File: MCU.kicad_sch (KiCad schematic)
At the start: 28 parts, among them J2 USB_C_Receptacle_USB2.0_16P, J8 FTSH-105-01-L-DV-K-A, U1 STM32H743VITx, Y1 Crystal_GND24

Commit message: LCD connector, backlight, other work
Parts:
- removed C12: 100n, Capacitor_SMD:C_0603_1608Metric_Pad1.08x0.95mm_HandSolder, symbol Device:C
- removed R5: 5.1k, Resistor_SMD:R_0603_1608Metric_Pad0.98x0.95mm_HandSolder, symbol Device:R
- removed S3: RKB2SJM250SMTR_LFS, RKB2SJM250SMTRLFS, symbol SamacSys_Parts:RKB2SJM250SMTR_LFS
- added C16, C17: 2.2u, Capacitor_SMD:C_0603_1608Metric_Pad1.08x0.95mm_HandSolder, symbol Device:C
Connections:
- net GND: now also U1.10 (VSS), U1.19 (VSSA), U1.26 (VSS), U1.49 (VSS), U1.74 (VSS), U1.99 (VSS), C16.2, C17.2
- net at U1.48 (VCAP): now also C17.1
- net at U1.73 (VCAP): now also C16.1
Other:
- removed sheet Indicator LED 1
- removed sheet Indicator LED 2

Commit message: preliminary complete schematic
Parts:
- added C33: 100n, Capacitor_SMD:C_0603_1608Metric_Pad1.08x0.95mm_HandSolder, symbol Device:C
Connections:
- net SWO is gone; now on net I2S_BCLK: J8.6
- net +3.3V: now also U1.100 (VDD), U1.11 (VDD), U1.27 (VDD), U1.50 (VDD), U1.75 (VDD), C33.1
- net BOOT0: now also U1.93 (PB7), U1.94 (BOOT0)
- net GND: now also C33.2
- net HSE_IN: now also U1.12 (PH0)
- net HSE_OUT: now also U1.13 (PH1)
- net NRST: now also U1.14 (NRST)
- net SWD_CLK: now also U1.76 (PA14)
- net SWD_IO: now also U1.72 (PA13)
- net USB+: now also U1.71 (PA12)
- net USB-: now also U1.70 (PA11)
- net LCD_R5: now reaches U1.15 (PC0)
- net SD_MOSI: now reaches U1.16 (PC1)
- net DPAD_A0: now reaches U1.17 (PC2_C)
- net DPAD_A1: now reaches U1.18 (PC3_C)
- net VDDA: now reaches U1.20 (VREF+)
- net VDDA: now also U1.21 (VDDA)
- net LCD_R2: now reaches U1.23 (PA1)
- net LCD_R1: now reaches U1.24 (PA2)
- net LCD_B5: now reaches U1.25 (PA3)
- net LCD_VSYNC: now reaches U1.28 (PA4)
- net LCD_R4: now reaches U1.29 (PA5)
- net LCD_G2: now reaches U1.30 (PA6)
- net I2S_SD: now reaches U1.31 (PA7)
- net V_SENSE_5: now reaches U1.32 (PC4)
- net LCD_R3: now reaches U1.34 (PB0)
- net V_SENSE_12: now reaches U1.35 (PB1)
- net BKLT_CTRL: now reaches U1.39 (PE9)
- net LCD_G3: now reaches U1.41 (PE11)
- net LCD_B4: now reaches U1.42 (PE12)
- net LCD_DE: now reaches U1.43 (PE13)
- net LCD_CLK: now reaches U1.44 (PE14)
- net LCD_R7: now reaches U1.45 (PE15)
- net LCD_G4: now reaches U1.46 (PB10)
- net LCD_G5: now reaches U1.47 (PB11)
- net SD_SCK: now reaches U1.52 (PB13)
- net SD_SCK: now also U1.80 (PC12)
- net SD_MISO: now reaches U1.53 (PB14)
- net SD_CS: now reaches U1.54 (PB15)
- net SD_WP: now reaches U1.55 (PD8)
- net SD_CD: now reaches U1.56 (PD9)
- net LCD_B3: now reaches U1.57 (PD10)
- net LCD_EN: now reaches U1.58 (PD11)
- net CTP_SCL: now reaches U1.59 (PD12)
- net CTP_SDA: now reaches U1.60 (PD13)
- net CTP_INT: now reaches U1.61 (PD14)
- net CTP_RST: now reaches U1.62 (PD15)
- net LCD_HSYNC: now reaches U1.63 (PC6)
- net LCD_G6: now reaches U1.64 (PC7)
- net SD_D0: now reaches U1.65 (PC8)
- net SD_D1: now reaches U1.66 (PC9)
- net LCD_R6: now reaches U1.67 (PA8)
- net I2S_WS: now reaches U1.77 (PA15)
- net SD_D2: now reaches U1.78 (PC10)
- net SD_D3: now reaches U1.79 (PC11)
- net DPAD_RX: now reaches U1.81 (PD0)
- net DPAD_TX: now reaches U1.82 (PD1)
- net SD_CMD: now reaches U1.83 (PD2)
- net LCD_G7: now reaches U1.84 (PD3)
- net LCD_B2: now reaches U1.87 (PD6)
- net I2S_BCLK: now reaches U1.89 (PB3)
- net LCD_B6: now reaches U1.95 (PB8)
- net LCD_B7: now reaches U1.96 (PB9)
- no-connect marks 4 -> 30

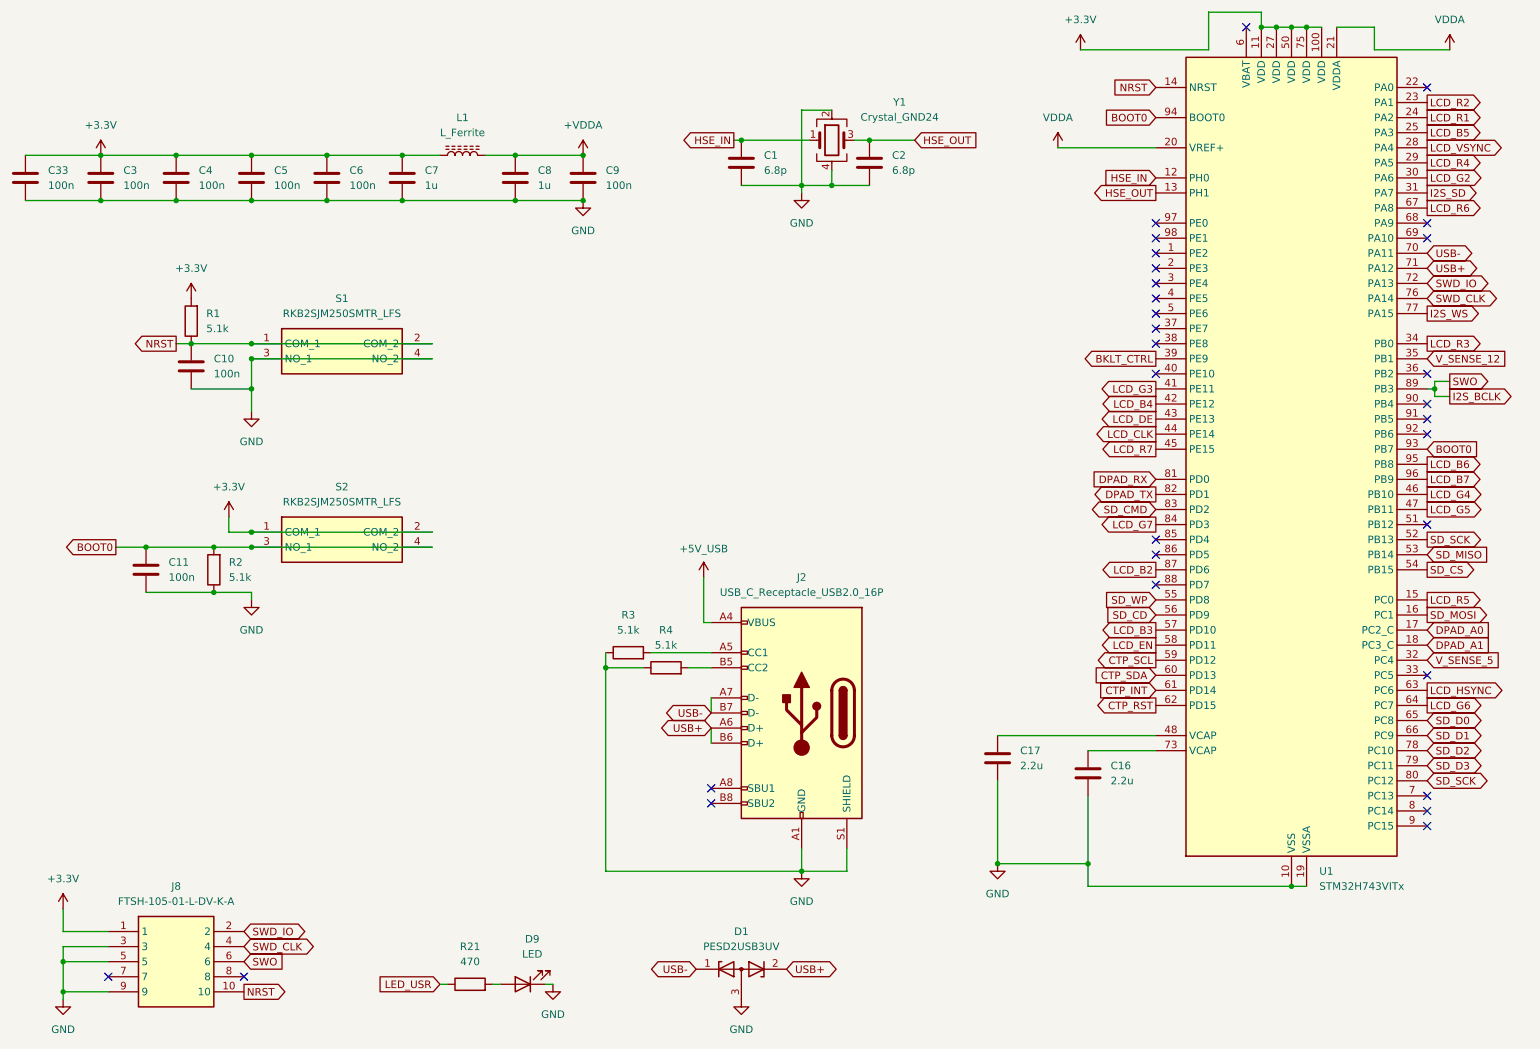
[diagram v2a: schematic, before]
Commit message: basic layout organization, fix +VDDA typo
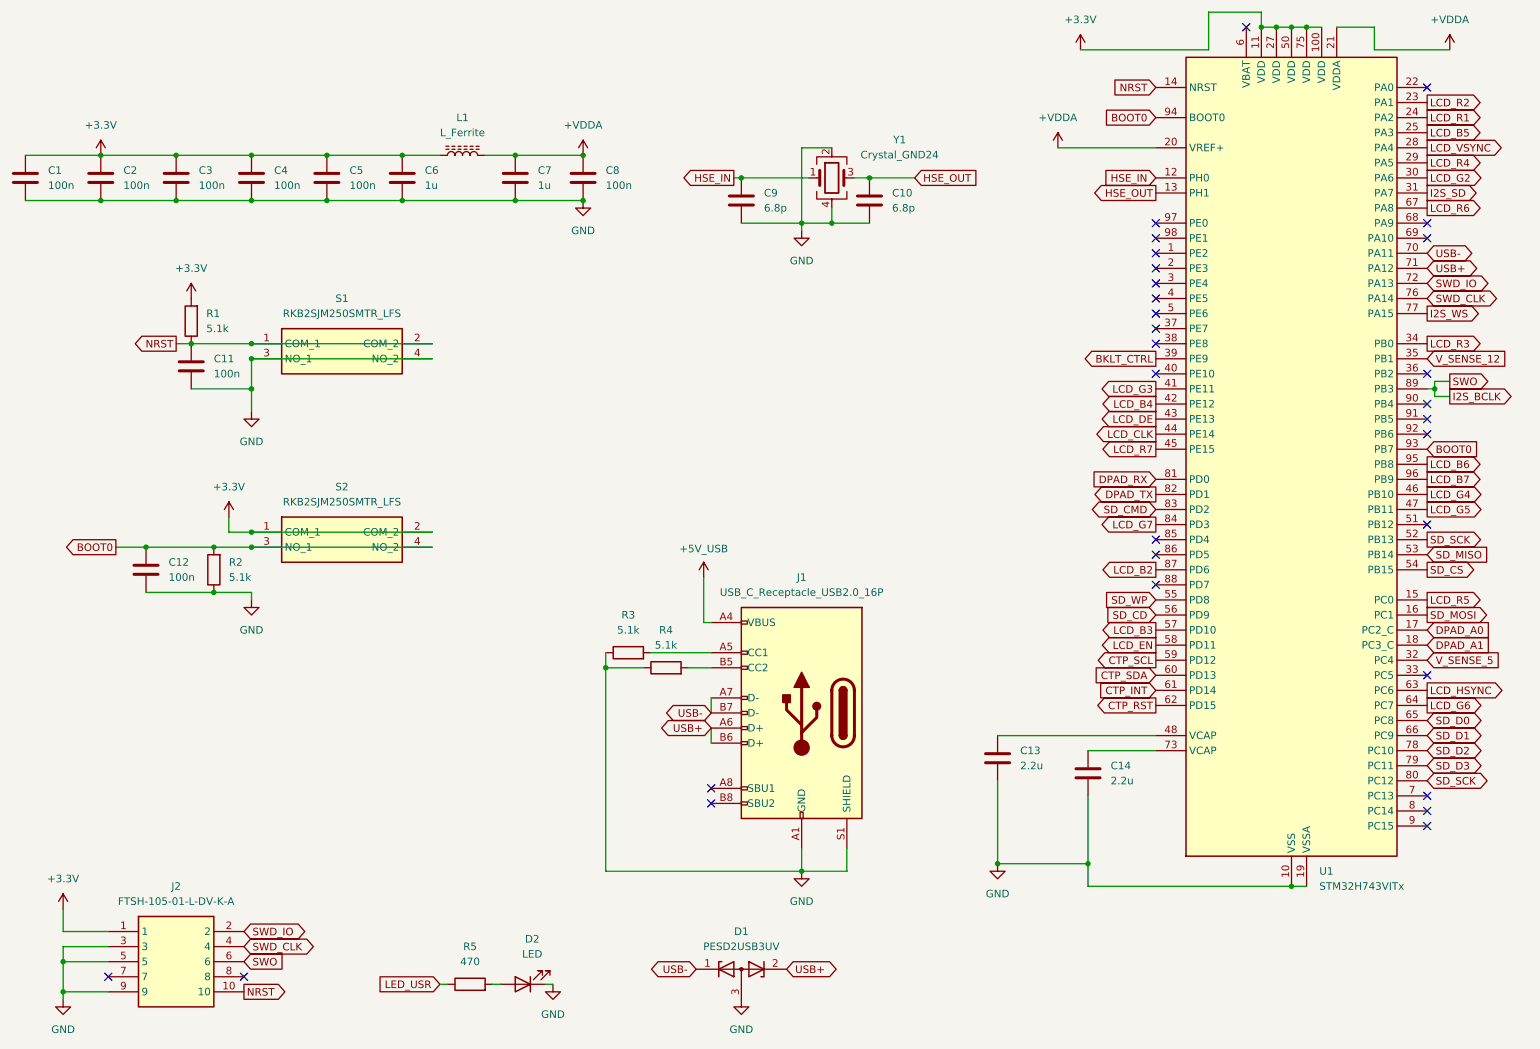
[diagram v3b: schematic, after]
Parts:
- renumbered C33 to C1, C2 to C10, C10 to C11, C11 to C12, C17 to C13, C16 to C14, C3 to C2, C4 to C3, C5 to C4, C6 to C5, C7 to C6, C8 to C7, C9 to C8, C1 to C9, D9 to D2, J2 to J1, J8 to J2, R21 to R5
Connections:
- net VDDA is gone; now on net +VDDA: U1.20 (VREF+), U1.21 (VDDA)
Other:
- moved on the sheet: C10, C9, Y1

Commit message: full preliminary layout
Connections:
- net FDCAN2_RX: now reaches U1.51 (PB12)
- net FDCAN2_TX: now reaches U1.92 (PB6)
- no-connect marks 30 -> 28
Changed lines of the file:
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@@
-	)
-	(no_connect
-		(at 261.62 85.09)
 	)
 	(no_connect
@@
 	(no_connect
 		(at 261.62 125.73)
-	)
-	(no_connect
-		(at 261.62 100.33)
 	)
 	(no_connect
@@
 		)
 	)
+	(global_label "FDCAN2_RX"
+		(shape input)
+		(at 261.62 100.33 0)
+		(fields_autoplaced yes)
+		(effects
+			(font
+				(size 1.27 1.27)
+			)
+			(justify left)
+		)
+		(property "Intersheetrefs" "${INTERSHEET_REFS}"
+			(at 275.3095 100.33 0)
+			(effects
+				(font
+					(size 1.27 1.27)
+				)
+				(justify left)
+				(hide yes)
+			)
+		)
+	)
 	(global_label "BOOT0"
 		(shape input)
@@
 			(effects
 				(font
+					(size 1.27 1.27)
+				)
+				(justify left)
+				(hide yes)
+			)
+		)
+	)
+	(global_label "FDCAN2_TX"
+		(shape output)
+		(at 261.62 85.09 0)
+		(fields_autoplaced yes)
+		(effects
+			(font
+				(size 1.27 1.27)
+			)
+			(justify left)
+		)
+		(property "Intersheetrefs" "${INTERSHEET_REFS}"
+			(at 275.0071 85.09 0)
+			(effects
+				(font

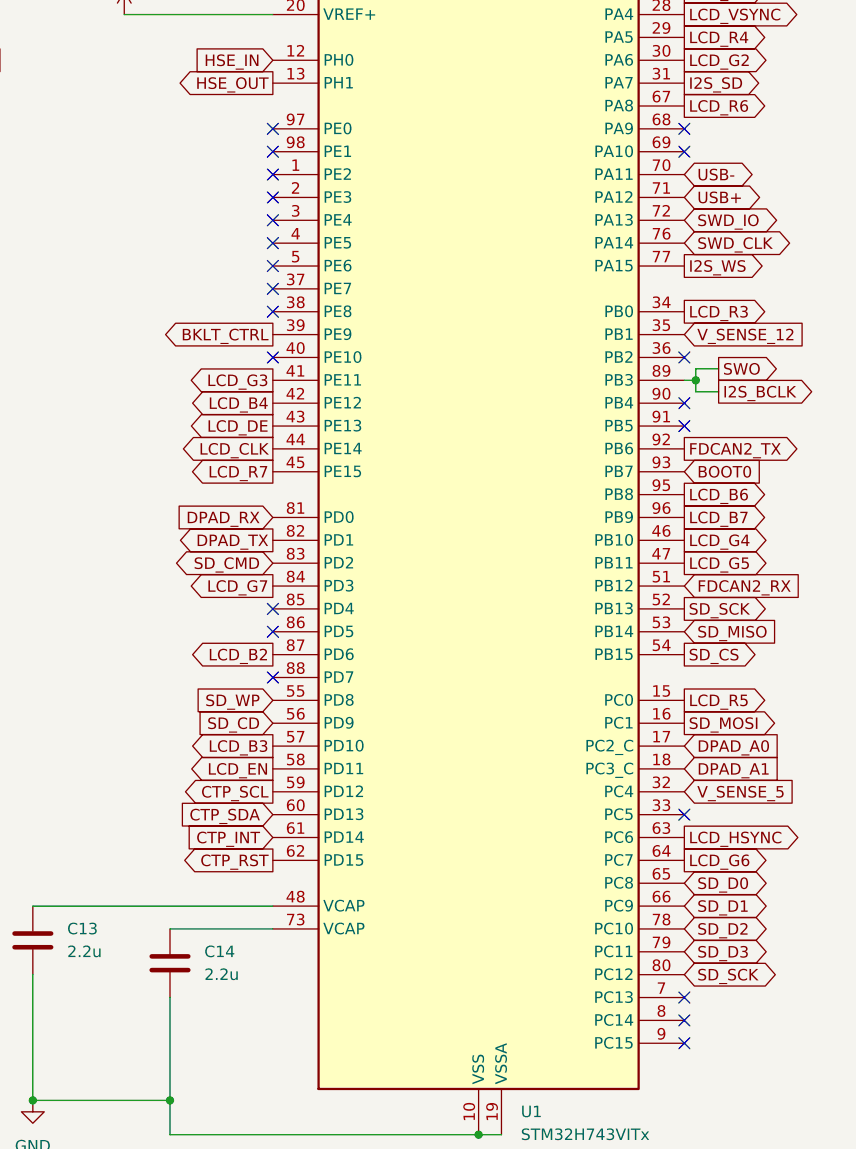
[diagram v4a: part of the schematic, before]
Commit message: 3.3v regulator changes, GPIO output fixes, layout changes
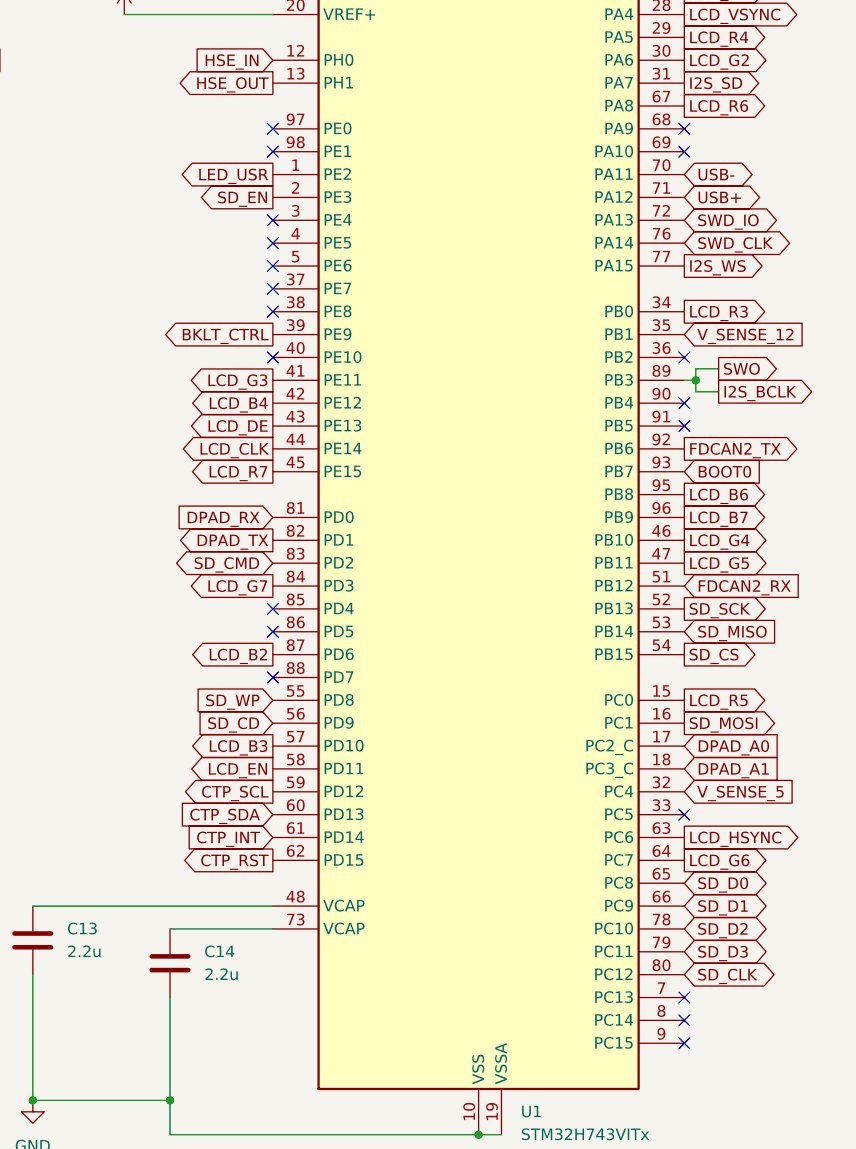
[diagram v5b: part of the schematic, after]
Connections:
- net LED_USR: now also U1.1 (PE2)
- net SD_SCK: no longer U1.80 (PC12)
- net SD_EN: now reaches U1.2 (PE3)
- new net SD_CLK: U1.80 (PC12)
- no-connect marks 28 -> 26
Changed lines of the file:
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@@
-	)
-	(no_connect
-		(at 215.9 57.15)
 	)
 	(no_connect
@@
 	(no_connect
 		(at 261.62 74.93)
-	)
-	(no_connect
-		(at 215.9 54.61)
 	)
 	(no_connect
@@
 		)
 	)
+	(global_label "LED_USR"
+		(shape output)
+		(at 215.9 54.61 180)
+		(fields_autoplaced yes)
+		(effects
+			(font
+				(size 1.27 1.27)
+			)
+			(justify right)
+		)
+		(property "Intersheetrefs" "${INTERSHEET_REFS}"
+			(at 204.6901 54.61 0)
+			(effects
+				(font
+					(size 1.27 1.27)
+				)
+				(justify right)
+				(hide yes)
+			)
+		)
+	)
 	(global_label "SD_MISO"
 		(shape input)
@@
 		)
 	)
+	(global_label "SD_EN"
+		(shape output)
+		(at 215.9 57.15 180)
+		(fields_autoplaced yes)
+		(effects
+			(font
+				(size 1.27 1.27)
+			)
+			(justify right)
+		)
+		(property "Intersheetrefs" "${INTERSHEET_REFS}"
+			(at 206.9882 57.15 0)
+			(effects
+				(font
+					(size 1.27 1.27)
+				)
+				(justify right)
+				(hide yes)
+			)
+		)
+	)
 	(global_label "HSE_IN"
 		(shape input)
@@
 		)
 	)
-	(global_label "SD_SCK"
+	(global_label "SD_CLK"
 		(shape bidirectional)
 		(at 261.62 143.51 0)
@@
 		)
 		(property "Intersheetrefs" "${INTERSHEET_REFS}"
-			(at 272.9131 143.51 0)
-			(effects
-				(font
+			(at 272.7317 143.51 0)
+			(effects
+				(font

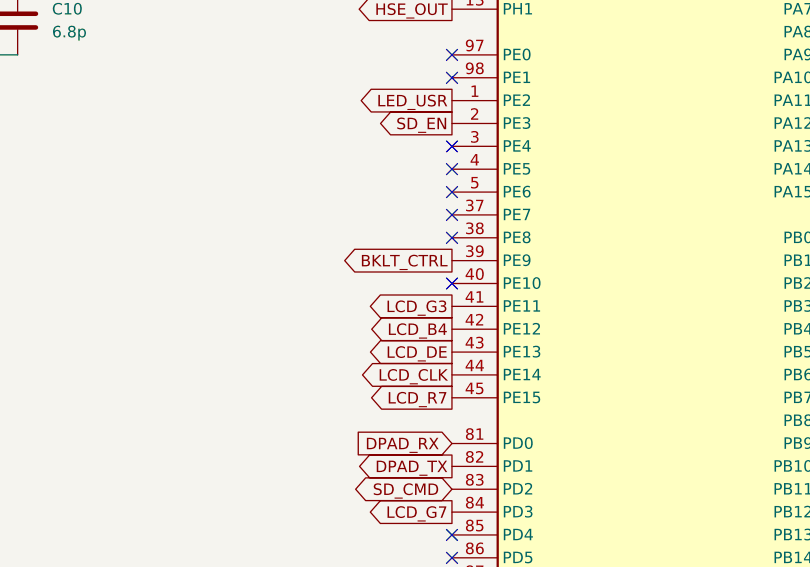
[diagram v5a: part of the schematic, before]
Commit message: finalized schematic, some routing
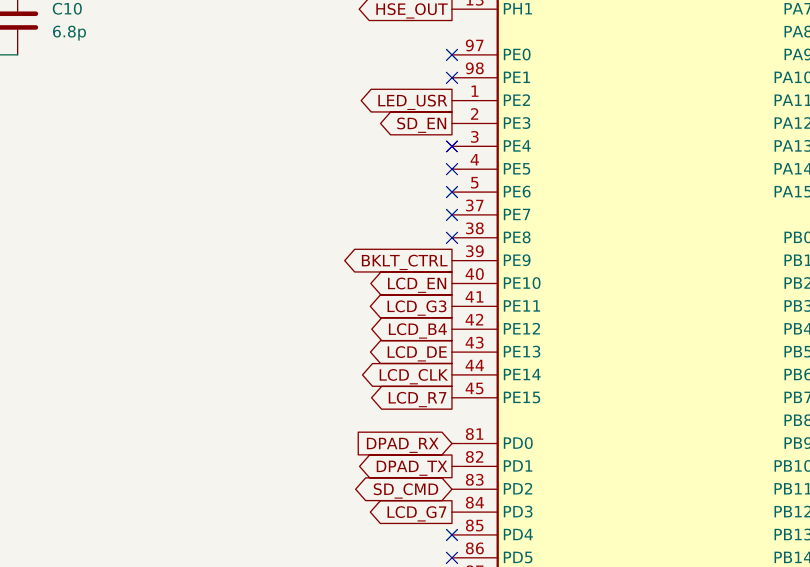
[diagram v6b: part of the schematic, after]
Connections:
- net LCD_EN: now also U1.40 (PE10)
- no-connect marks 26 -> 25
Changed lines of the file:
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@@
-	)
-	(no_connect
-		(at 215.9 74.93)
 	)
 	(no_connect
@@
 				(hide yes)
 			)
+		)
+	)
+	(global_label "LCD_EN"
+		(shape output)
+		(at 215.9 74.93 180)
+		(fields_autoplaced yes)
+		(effects
+			(font
+				(size 1.27 1.27)
+			)
+			(justify right)
+		)
+		(property "Intersheetrefs" "${INTERSHEET_REFS}"
+			(at 205.8996 74.93 0)
+			(effects
+				(font
+					(size 1.27 1.27)
+				)
+				(justify right)
+				(hide yes)
+			)

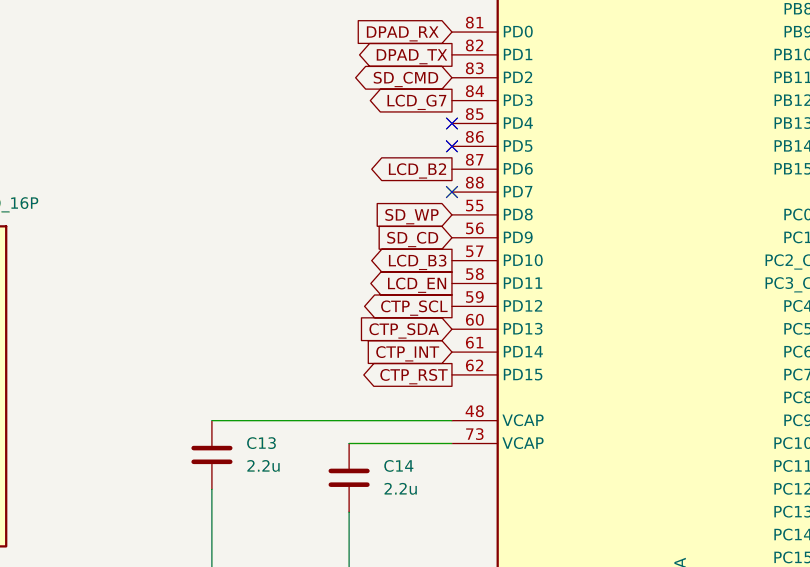
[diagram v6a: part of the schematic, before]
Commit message: fix duplicate LCD_EN pin, initial ZIF routing
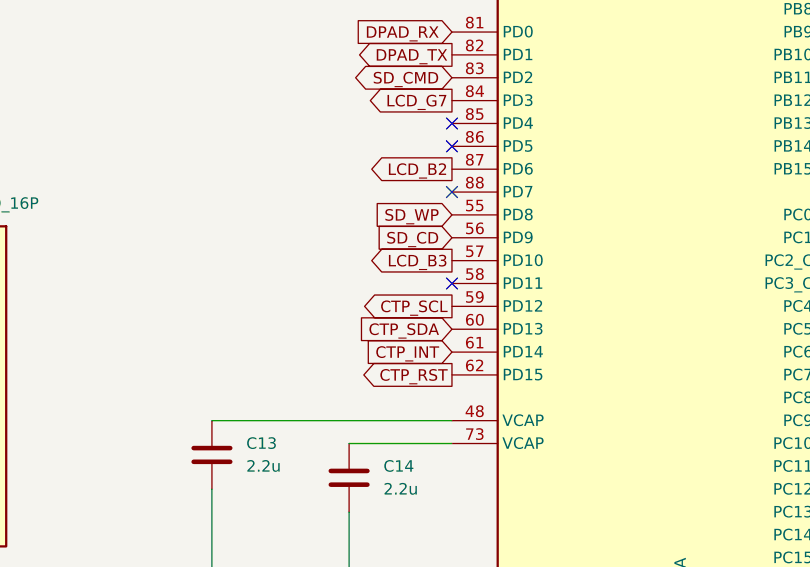
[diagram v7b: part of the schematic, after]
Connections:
- net LCD_EN: no longer U1.58 (PD11)
- no-connect marks 25 -> 26
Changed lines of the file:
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@@
+	)
+	(no_connect
+		(at 215.9 120.65)
 	)
 	(no_connect
@@
 			(effects
 				(font
-					(size 1.27 1.27)
-				)
-				(justify right)
-				(hide yes)
-			)
-		)
-	)
-	(global_label "LCD_EN"
-		(shape output)
-		(at 215.9 120.65 180)
-		(fields_autoplaced yes)
-		(effects
-			(font
-				(size 1.27 1.27)
-			)
-			(justify right)
-		)
-		(property "Intersheetrefs" "${INTERSHEET_REFS}"
-			(at 205.8996 120.65 0)
-			(effects
-				(font

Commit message: r1 final (see changelog.md)
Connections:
- net SAI_FS: now reaches U1.3 (PE4)
- net SAI_SCK: now reaches U1.4 (PE5)
- net SAI_SD: now reaches U1.5 (PE6)
- no-connect marks 26 -> 23
